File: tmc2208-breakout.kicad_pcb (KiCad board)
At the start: 2 copper layers, 31 x 36 mm, 40 parts, among them J1 Conn_01x11, J3 Conn_01x04, J4 Conn_01x02, U1 TMC2208-LA

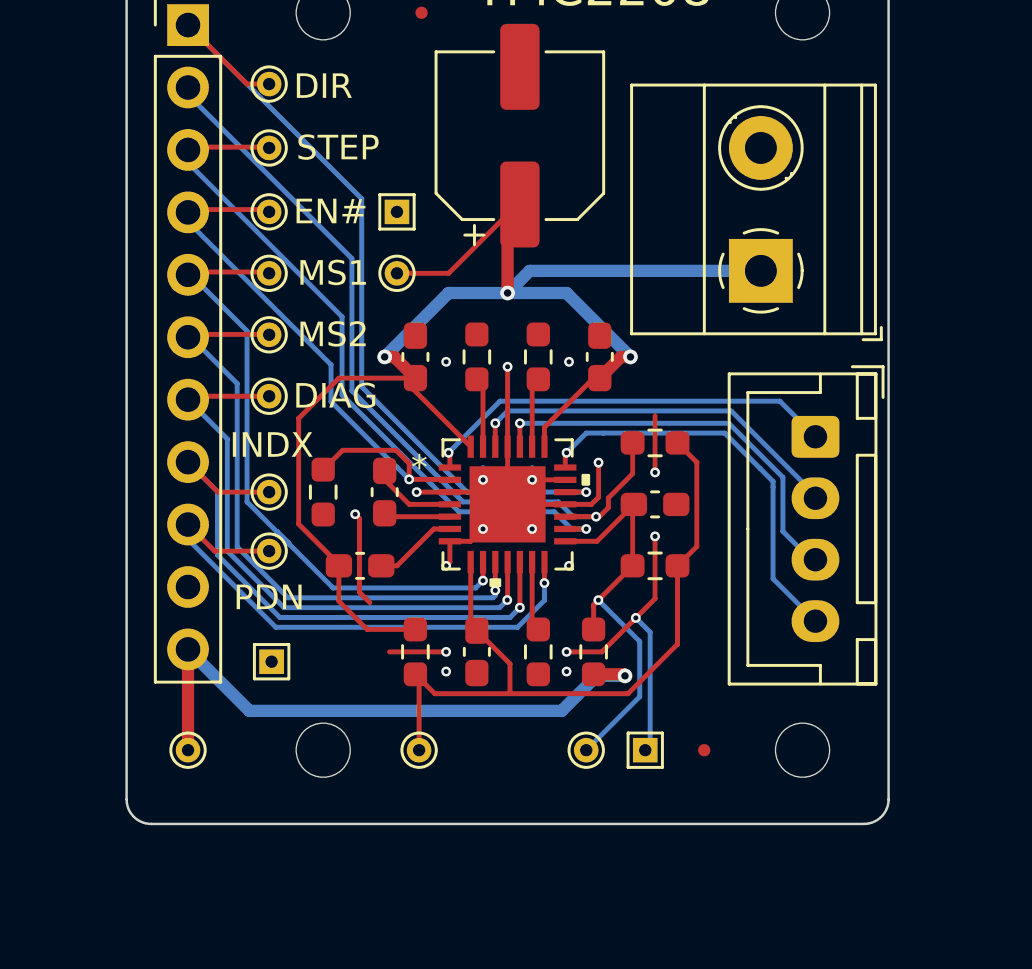
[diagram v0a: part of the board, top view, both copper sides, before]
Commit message: added LEDs for EN# and STEP
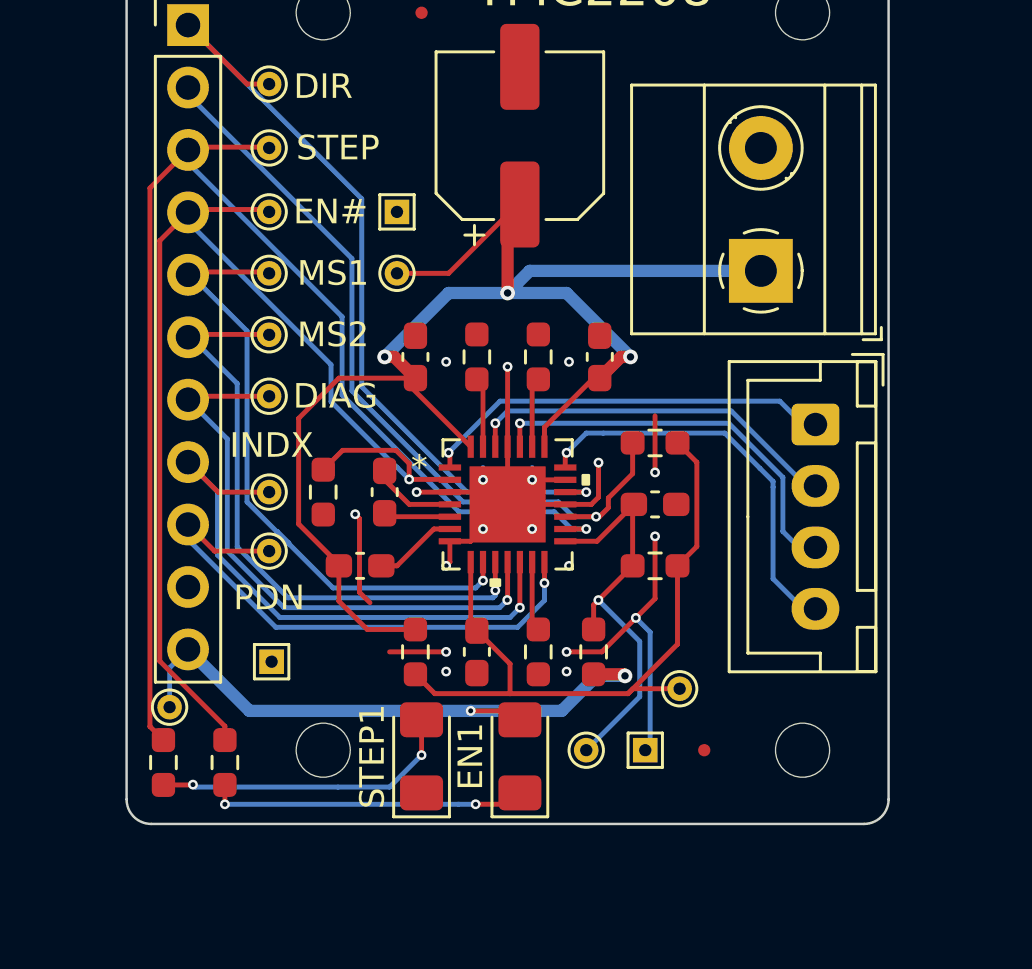
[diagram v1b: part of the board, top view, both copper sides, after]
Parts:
- added EN1: RED, LED_SMD:LED_1206_3216Metric_Pad1.42x1.75mm_HandSolder, F.Cu at (157.5, 71.2)
- added R10: 100, Resistor_SMD:R_0603_1608Metric_Pad0.98x0.95mm_HandSolder, F.Cu at (143.0, 71.5)
- added R9: 100, Resistor_SMD:R_0603_1608Metric_Pad0.98x0.95mm_HandSolder, F.Cu at (145.5, 71.5)
- added STEP1: GREEN, LED_SMD:LED_1206_3216Metric_Pad1.42x1.75mm_HandSolder, F.Cu at (153.5, 71.2)
- moved TP15 10.9 mm to (164.0, 68.5)
- moved TP16 1.90 mm to (143.2, 69.2)
- moved J3 0.50 mm to (169.5, 57.8)
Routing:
- net /STEP: track 28.4 -> 53.3 mm
- net /EN#: track 24.4 -> 47.4 mm
- net Net-(EN1-Pad1): track 0.00 -> 13.0 mm, vias 0 -> 2
- net Net-(STEP1-Pad2): track 0.00 -> 12.5 mm, vias 0 -> 2
- net +5V: track 29.8 -> 28.9 mm
- net +3V3: track 24.8 -> 25.5 mm, vias 1 -> 2
